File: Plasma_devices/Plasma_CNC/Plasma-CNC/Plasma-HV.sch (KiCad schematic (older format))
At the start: 0 parts

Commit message: Updaged electrical
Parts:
- added J?: Conn_01x02_Female, symbol Connector:Conn_01x02_Female
- added K?: FINDER-49.61.9.024.0050, Relay_THT:Relay_DPDT_Finder_40.52, symbol Relay:FINDER-40.52
- added PS?: MW S-350-24, Converter_ACDC:Converter_ACDC_MeanWell_IRM-20-xx_THT, symbol Converter_ACDC:IRM-20-24
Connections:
- net HVon: now also K?.A1
- net LINE: now also PS?.1 (AC/L)
- net NEUTRAL: now also PS?.2 (AC/N)
- net SIG-GND: now also K?.A2
- new net Latch_HV_enbl/+Vout: K?.24
- new net Latch_HV_enbl/-Vout: K?.14
- new net ZVS_module/+LVin: K?.21
- new net ZVS_module/-LVin: K?.11
- new net ZVS_module/HVACout1: J?.1 (Pin_1)
- new net ZVS_module/HVACout2: J?.2 (Pin_2)
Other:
- note added: "External HV enable"
- note added: "HV output\nto plasma jet"
- note added: "Mains to low voltage"
- note added: "Self-holding relay \n/ safety latch"
- note added: "Voltage regulator"
- note added: "ZVS module\nHV generation"
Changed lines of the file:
@@
 $Descr A4 11693 8268
 encoding utf-8
-Sheet 2 6
+Sheet 2 8
 Title ""
 Date ""
@@
 Comment4 ""
 $EndDescr
-Text HLabel 1450 1100 0    50   Input ~ 0
+Text HLabel 1450 1600 0    50   Input ~ 0
 LINE
-Text HLabel 1450 1250 0    50   Input ~ 0
+Text HLabel 1450 1750 0    50   Input ~ 0
 NEUTRAL
-Text HLabel 1450 1400 0    50   Input ~ 0
+Text HLabel 1450 1900 0    50   Input ~ 0
 PE
-Text HLabel 1450 1750 0    50   Input ~ 0
+Text HLabel 6500 2500 3    50   Input ~ 0
 HVon
-Text HLabel 1450 1850 0    50   Input ~ 0
+Text HLabel 3700 2150 0    50   Input ~ 0
 Control
-Text HLabel 1450 1950 0    50   Input ~ 0
+Text HLabel 7500 2500 3    50   Input ~ 0
 SIG-GND
+Text Notes 5150 750  0    50   ~ 0
+Self-holding relay \n/ safety latch
+$Comp
+L Converter_ACDC:IRM-20-24 PS?
+U 1 1 5F63C51A
+P 2050 1650
+F 0 "PS?" H 2050 1975 50  0000 C CNN
+F 1 "MW S-350-24" H 2050 1884 50  0000 C CNN
+F 2 "Converter_ACDC:Converter_ACDC_MeanWell_IRM-20-xx_THT" H 2050 1350 50  0001 C CNN
+F 3 "http://www.meanwell.com/Upload/PDF/IRM-20/IRM-20-SPEC.PDF" H 2450 1300 50  0001 C CNN
+	1    2050 1650
+	1    0    0    -1
+$EndComp
+$Comp
+L Relay:FINDER-40.52 K?
+U 1 1 5F63EFD9
+P 7000 2050
+F 0 "K?" V 7767 2050 50  0000 C CNN
+F 1 "FINDER-49.61.9.024.0050" V 7676 2050 50  0000 C CNN
+F 2 "Relay_THT:Relay_DPDT_Finder_40.52" H 8350 2020 50  0001 C CNN
+F 3 "http://gfinder.findernet.com/assets/Series/353/S40EN.pdf" H 7000 2050 50  0001 C CNN
+	1    7000 2050
+	0    -1   -1   0
+$EndComp
+Text Notes 6600 750  0    50   ~ 0
+External HV enable
+$Comp
+L power:GND #PWR?
+U 1 1 5F642692
+P 1650 1900
+F 0 "#PWR?" H 1650 1650 50  0001 C CNN
+F 1 "GND" H 1655 1727 50  0000 C CNN
+F 2 "" H 1650 1900 50  0001 C CNN
+F 3 "" H 1650 1900 50  0001 C CNN
+	1    1650 1900
+	1    0    0    -1
+$EndComp
+Wire Wire Line
+	1450 1750 1650 1750
+Wire Wire Line
+	1650 1900 1450 1900
+Wire Wire Line
+	1450 1600 1650 1600
+Wire Wire Line
+	1650 1600 1650 1550
+Text Notes 1700 750  0    50   ~ 0
+Mains to low voltage
+Text Notes 3450 750  0    50   ~ 0
+Voltage regulator
+Text Notes 8250 750  0    50   ~ 0
+ZVS module\nHV generation
+$Sheet
+S 8000 1500 1000 500
+U 5F6466E4
+F0 "ZVS_module" 50
+F1 "ZVS_module.sch" 50
+F2 "+LVin" I L 8000 1650 50
+F3 "-LVin" I L 8000 1850 50
+F4 "HVACout1" O R 9000 1650 50
+F5 "HVACout2" O R 9000 1850 50
+$EndSheet
+$Sheet
+S 5000 1500 1000 500
+U 5F64687A
+F0 "Latch_HV_enbl" 50
+F1 "Latch_HV_enbl.sch" 50
+F2 "+Vin" I L 5000 1650 50
+F3 "-Vin" I L 5000 1850 50
+F4 "+Vout" O R 6000 1650 50
+F5 "-Vout" O R 6000 1850 50
+$EndSheet
+Wire Wire Line
+	6500 2500 6500 2450
+Wire Wire Line
+	6500 2450 6700 2450
+Wire Wire Line
+	7300 2450 7500 2450
+Wire Wire Line
+	7500 2450 7500 2500
+Wire Wire Line
+	6000 1850 6450 1850
+Wire Wire Line
+	6450 1850 6450 1950
+Wire Wire Line
+	6450 1950 6700 1950
+Wire Wire Line
+	6000 1650 6450 1650
+Wire Wire Line
+	6450 1650 6450 1550
+Wire Wire Line
+	6450 1550 6700 1550
+Wire Wire Line
+	7300 1650 8000 1650
+Wire Wire Line
+	8000 1850 7500 1850
+Wire Wire Line
+	7500 1850 7500 2050
+Wire Wire Line
+	7500 2050 7300 2050
+$Comp
+L Connector:Conn_01x02_Female J?
+U 1 1 5F6497F1
+P 9700 1650
+F 0 "J?" H 9728 1626 50  0000 L CNN
+F 1 "Conn_01x02_Female" H 9728 1535 50  0000 L CNN
+F 2 "" H 9700 1650 50  0001 C CNN
+F 3 "~" H 9700 1650 50  0001 C CNN
+	1    9700 1650
+	1    0    0    -1
+$EndComp
+Text Notes 9500 750  0    50   ~ 0
+HV output\nto plasma jet
+Wire Wire Line
+	9500 1650 9000 1650
+Wire Wire Line
+	9500 1750 9250 1750
+Wire Wire Line
+	9250 1750 9250 1850
+Wire Wire Line
+	9250 1850 9000 1850
 $EndSCHEMATC

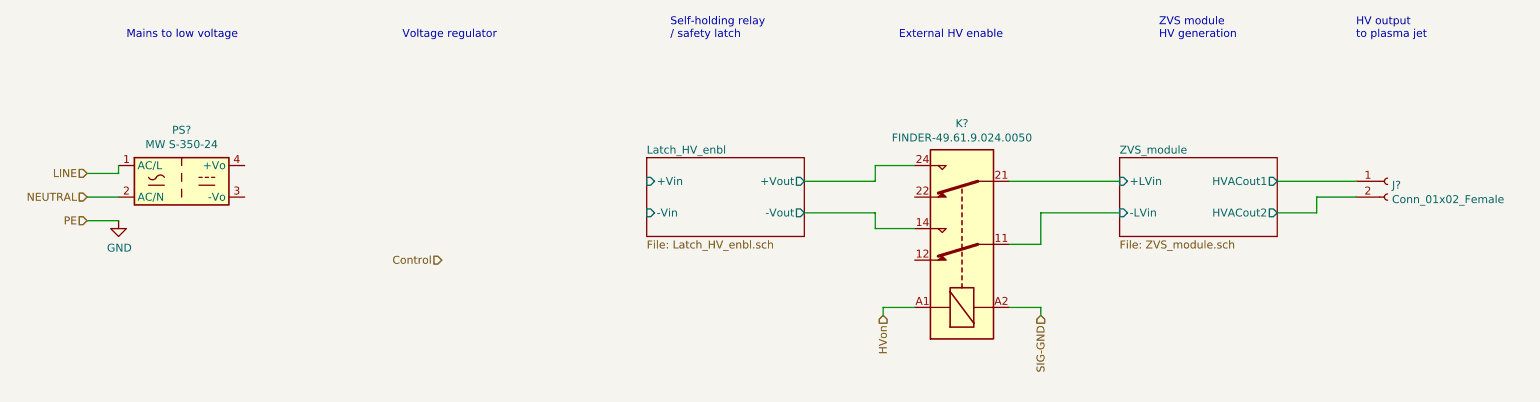
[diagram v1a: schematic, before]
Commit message: DVS module included
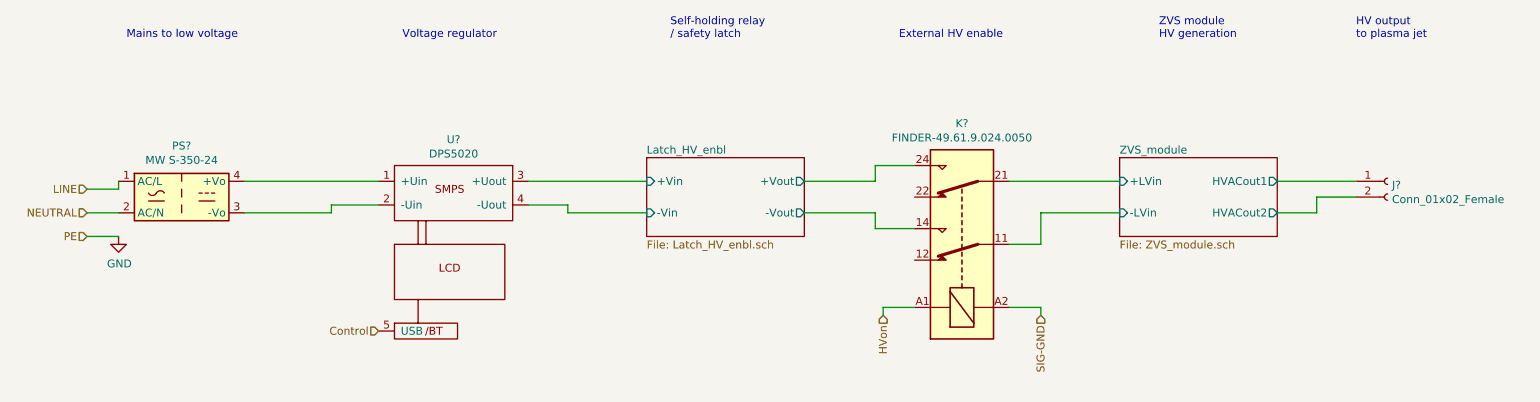
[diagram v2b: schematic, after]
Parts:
- added U?: DPS5020, symbol Plasma-CNC:DPS5020
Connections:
- net Control: now also U?.5 (USB)
- net Latch_HV_enbl/+Vin: now also U?.3 (+Uout)
- net Latch_HV_enbl/-Vin: now also U?.4 (-Uout)
- net at PS?.3 (-Vo): now also U?.2 (-Uin)
- net at PS?.4 (+Vo): now also U?.1 (+Uin)
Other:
- moved on the sheet: PS?
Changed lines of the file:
@@
 Comment4 ""
 $EndDescr
-Text HLabel 1450 1600 0    50   Input ~ 0
+Text HLabel 1450 1700 0    50   Input ~ 0
 LINE
-Text HLabel 1450 1750 0    50   Input ~ 0
+Text HLabel 1450 1850 0    50   Input ~ 0
 NEUTRAL
-Text HLabel 1450 1900 0    50   Input ~ 0
+Text HLabel 1450 2000 0    50   Input ~ 0
 PE
 Text HLabel 6500 2500 3    50   Input ~ 0
 HVon
-Text HLabel 3700 2150 0    50   Input ~ 0
+Text HLabel 3300 2600 0    50   Input ~ 0
 Control
 Text HLabel 7500 2500 3    50   Input ~ 0
@@
 L Converter_ACDC:IRM-20-24 PS?
 U 1 1 5F63C51A
-P 2050 1650
-F 0 "PS?" H 2050 1975 50  0000 C CNN
-F 1 "MW S-350-24" H 2050 1884 50  0000 C CNN
-F 2 "Converter_ACDC:Converter_ACDC_MeanWell_IRM-20-xx_THT" H 2050 1350 50  0001 C CNN
-F 3 "http://www.meanwell.com/Upload/PDF/IRM-20/IRM-20-SPEC.PDF" H 2450 1300 50  0001 C CNN
-	1    2050 1650
+P 2050 1750
+F 0 "PS?" H 2050 2075 50  0000 C CNN
+F 1 "MW S-350-24" H 2050 1984 50  0000 C CNN
+F 2 "Converter_ACDC:Converter_ACDC_MeanWell_IRM-20-xx_THT" H 2050 1450 50  0001 C CNN
+F 3 "http://www.meanwell.com/Upload/PDF/IRM-20/IRM-20-SPEC.PDF" H 2450 1400 50  0001 C CNN
+	1    2050 1750
 	1    0    0    -1
 $EndComp
@@
 L power:GND #PWR?
 U 1 1 5F642692
-P 1650 1900
-F 0 "#PWR?" H 1650 1650 50  0001 C CNN
-F 1 "GND" H 1655 1727 50  0000 C CNN
-F 2 "" H 1650 1900 50  0001 C CNN
-F 3 "" H 1650 1900 50  0001 C CNN
-	1    1650 1900
+P 1650 2000
+F 0 "#PWR?" H 1650 1750 50  0001 C CNN
+F 1 "GND" H 1655 1827 50  0000 C CNN
+F 2 "" H 1650 2000 50  0001 C CNN
+F 3 "" H 1650 2000 50  0001 C CNN
+	1    1650 2000
 	1    0    0    -1
 $EndComp
 Wire Wire Line
-	1450 1750 1650 1750
+	1450 1850 1650 1850
 Wire Wire Line
-	1650 1900 1450 1900
+	1650 2000 1450 2000
 Wire Wire Line
-	1450 1600 1650 1600
+	1450 1700 1650 1700
 Wire Wire Line
-	1650 1600 1650 1550
+	1650 1700 1650 1650
 Text Notes 1700 750  0    50   ~ 0
 Mains to low voltage
@@
 Wire Wire Line
 	9250 1850 9000 1850
+$Comp
+L Plasma-CNC:DPS5020 U?
+U 1 1 5F6A1C93
+P 3750 1750
+F 0 "U?" H 3775 2115 50  0000 C CNN
+F 1 "DPS5020" H 3775 2024 50  0000 C CNN
+F 2 "" H 3750 1750 50  0001 C CNN
+F 3 "" H 3750 1750 50  0001 C CNN
+	1    3750 1750
+	1    0    0    -1
+$EndComp
+Wire Wire Line
+	2450 1650 3300 1650
+Wire Wire Line
+	4250 1650 5000 1650
+Wire Wire Line
+	2450 1850 3000 1850
+Wire Wire Line
+	3000 1850 3000 1800
+Wire Wire Line
+	3000 1800 3300 1800
+Wire Wire Line
+	4250 1800 4500 1800
+Wire Wire Line
+	4500 1800 4500 1850
+Wire Wire Line
+	4500 1850 5000 1850
 $EndSCHEMATC
